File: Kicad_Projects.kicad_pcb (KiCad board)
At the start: 2 copper layers, 100.3 x 50.8 mm, 30 parts, among them J1 Ent. 15Vca, J2 Sal. Vcc Voltimetro/Amperimet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, J3 Sal. Tension regulable, J4 Sal. Amperimetro, Q1 BD137, Q2 TIP3055G, U1 LM723_DIP14

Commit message: Mejoras en PCB
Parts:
- R5: value 820 -> 1200
- moved D6 78.4 mm to (135.6, 106.2)
- moved D5 67.2 mm to (107.7, 105.4), turned to -90 degrees
- moved J2 44.7 mm to (95.0, 117.6), turned to 180 degrees
- moved C4 41.1 mm to (112.0, 92.2), turned to -90 degrees
- moved C6 35.6 mm to (159.4, 87.8), turned to 180 degrees
- moved D7 35.4 mm to (151.4, 95.2), turned to -90 degrees
- moved RV2 34.3 mm to (148.5, 76.2), turned to 180 degrees
- moved U1 29.5 mm to (132.3, 87.6), turned to -90 degrees
- moved R3 28.8 mm to (147.1, 95.3), turned to 180 degrees
- moved R2 25.3 mm to (116.3, 101.1), turned to 180 degrees
- moved C5 23.9 mm to (134.0, 97.9), turned to 180 degrees
- moved R4 22.3 mm to (136.9, 90.8)
- moved HS1 22.0 mm to (130.8, 115.6)
- moved Q2 22.0 mm to (136.3, 112.2)
- moved 10k1 21.6 mm to (109.3, 80.6), turned to 90 degrees
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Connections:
- net Net-(C6-Pad1) renamed Vout
- net Net-(D1-Pad2) renamed AC_F
- net Net-(D2-Pad2) renamed AC_N
- net Net-(D6-Pad2) renamed TBJ_Out
- net Net-(J3-Pad2) renamed Vout_amp
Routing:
- net +VDC: track 0.00 -> 163.4 mm
- net TBJ_Out: track 0.00 -> 87.3 mm
- net Vout: track 0.00 -> 86.7 mm
- net AC_F: track 0.00 -> 42.8 mm
- net AC_N: track 0.00 -> 41.1 mm
- net Net-(Q1-Pad1): track 0.00 -> 27.2 mm
- net Net-(C5-Pad1): track 0.00 -> 24.1 mm
- net Net-(10k1-Pad2): track 0.00 -> 18.8 mm
- net Net-(RV1-Pad2): track 0.00 -> 15.5 mm
- net Net-(10k1-Pad1): track 0.00 -> 14.5 mm
- net Net-(D5-Pad1): track 0.00 -> 11.3 mm
- net Net-(R5-Pad2): track 0.00 -> 10.6 mm
- net Net-(R5-Pad1): track 0.00 -> 8.00 mm
- net Net-(10k1-Pad3): track 0.00 -> 7.95 mm
- net Vout_amp: track 0.00 -> 6.86 mm
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- added copper zone on F.Cu, net GND

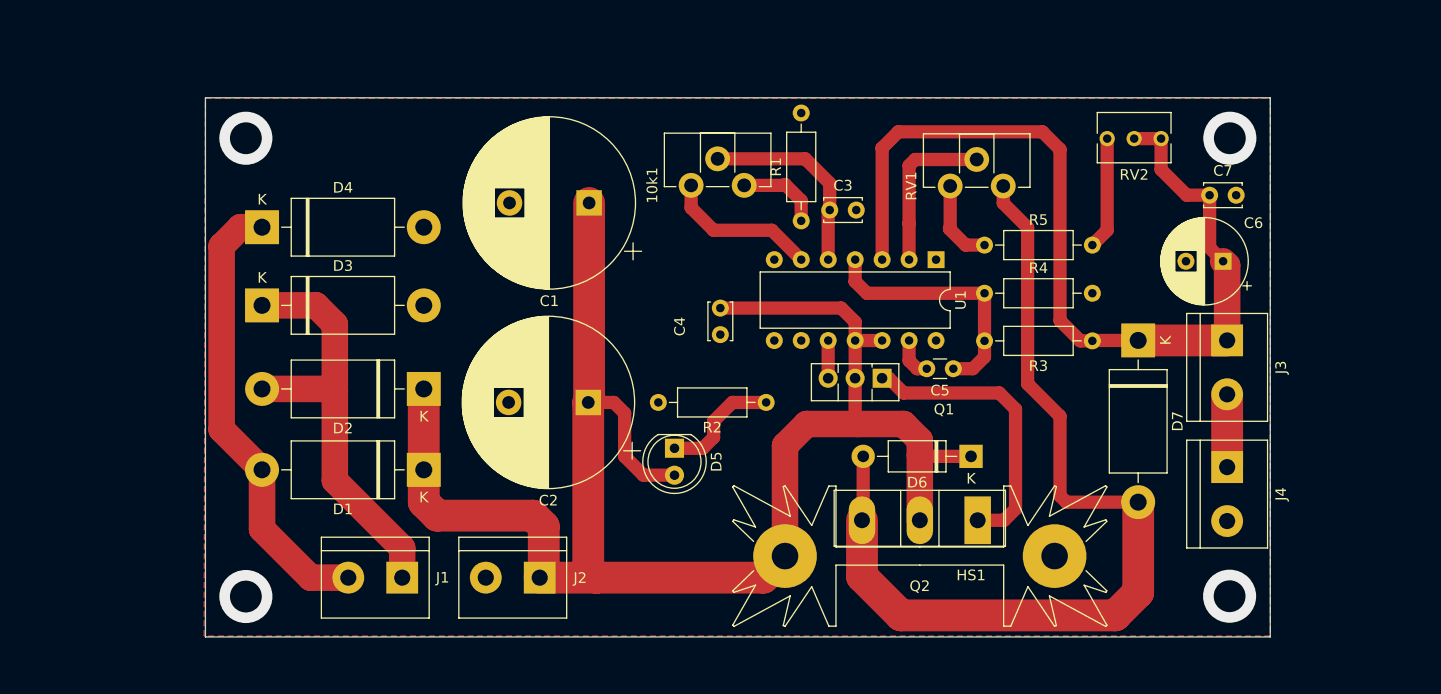
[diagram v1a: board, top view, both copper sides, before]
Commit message: Agregado de jumper
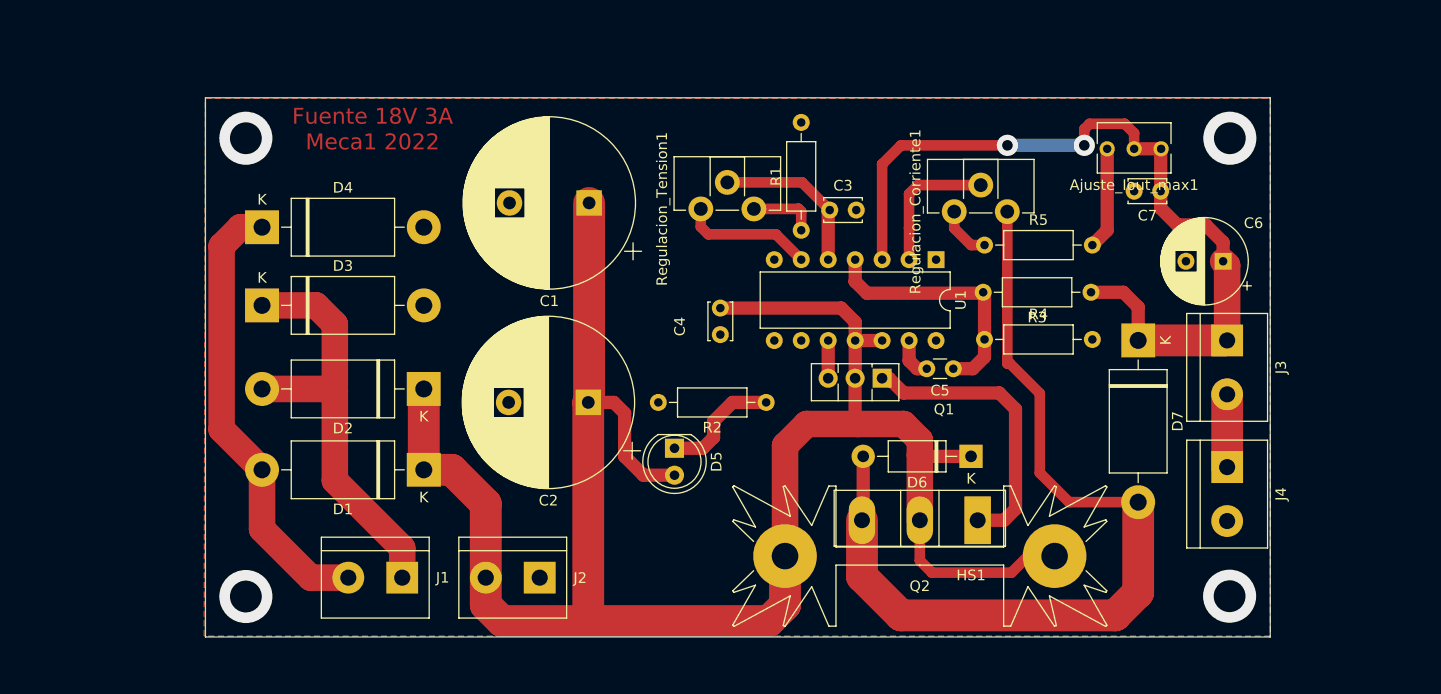
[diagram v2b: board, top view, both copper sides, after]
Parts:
- J2: value Sal. Vcc Voltimetro/Amperimetro -> Vcc_Volt/Amper
- J3: value Sal. Tension regulable -> Vout
- J4: value Sal. Amperimetro -> Amperimetro
- Regulacion_Tension1: renamed from 10k1; value R_Potentiometer -> 10k
- moved C7 4.63 mm to (153.5, 81.2), turned to 180 degrees
- moved R3 4.58 mm to (146.9, 90.7)
- moved R4 4.35 mm to (136.9, 95.2)
- moved Regulacion_Corriente1 2.44 mm to (134.1, 83.1)
- moved Regulacion_Tension1 2.40 mm to (110.2, 82.9)
- moved Ajuste_Iout_max1 0.96 mm to (148.5, 77.2)
- moved R1 0.89 mm to (119.6, 84.9)
- renumbered RV2 to Ajuste_Iout_max1, RV1 to Regulacion_Corriente1
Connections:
- J2 pad 1: +VDC -> GND
- J2 pad 2: GND -> +VDC
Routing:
- net +VDC: track 163.4 -> 190.0 mm
- net Vout: track 86.7 -> 78.4 mm, vias 0 -> 2
- net Net-(Regulacion_Tension1-Pad2): track 18.8 -> 15.5 mm
- net Net-(R5-Pad1): track 8.00 -> 5.08 mm
- net TBJ_Out: track 87.3 -> 84.8 mm
- net Net-(Regulacion_Corriente1-Pad2): track 15.5 -> 13.3 mm
- net Net-(Regulacion_Tension1-Pad1): track 14.5 -> 12.4 mm
- net Net-(Regulacion_Tension1-Pad3): track 7.95 -> 6.49 mm
- net Net-(R5-Pad2): track 10.6 -> 9.65 mm
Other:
- board text added: "Fuente 18V 3A Meca1 2022"
- board text added: "Fuente 18V 3A Mecatronica 1 -FRC- UTN"
